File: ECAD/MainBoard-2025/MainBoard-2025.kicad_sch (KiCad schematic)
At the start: 61 parts, among them J1 XT60, J11 Conn_01x04, J12 Conn_01x04, J15 Conn_01x02, J16 XT30, J18 Conn_01x02, J2 Conn_01x04, J20 BAU, J21 BAU, J22 Conn_01x04, J23 Conn_01x02, J26 BAU, J28 Conn_01x02, J3 Conn_01x04, J4 Conn_01x02, J7 XT30, J8 Conn_01x02, J9 Conn_01x02, K2 FINDER-36.11, U2 R-78B3.3-2.0, U3 R-78B12-2.0, U4 R-78B5.0-2.0, U5 Teensy4.1

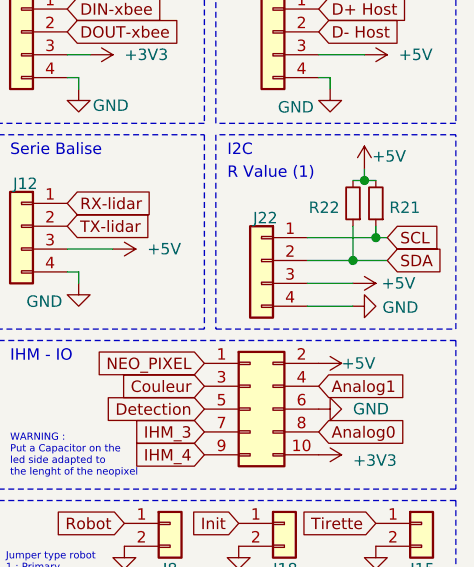
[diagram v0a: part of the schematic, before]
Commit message: new board cut edge and new robot frames
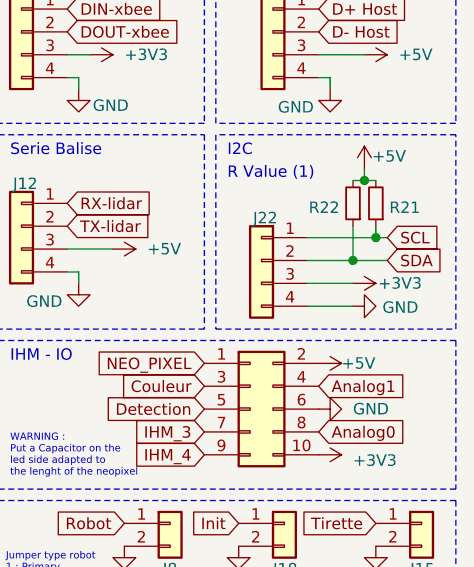
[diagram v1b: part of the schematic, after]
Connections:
- net +3V3: now also J22.3 (Pin_3)
- net +5V: no longer J22.3 (Pin_3)
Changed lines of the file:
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@@
 	)
 	(symbol
+		(lib_id "power:+3V3")
+		(at 271.78 82.55 270)
+		(unit 1)
+		(exclude_from_sim no)
+		(in_bom yes)
+		(on_board yes)
+		(dnp no)
+		(property "Reference" "#PWR044"
+			(at 267.97 82.55 0)
+			(effects
+				(font
+					(size 1.27 1.27)
+				)
+				(hide yes)
+			)
+		)
+		(property "Value" "+3V3"
+			(at 274.574 82.55 90)
+			(effects
+				(font
+					(size 1.27 1.27)
+				)
+				(justify left)
+			)
+		)
+		(property "Footprint" ""
+			(at 271.78 82.55 0)
+			(effects
+				(font
+					(size 1.27 1.27)
+				)
+				(hide yes)
+			)
+		)
+		(property "Datasheet" ""
+			(at 271.78 82.55 0)
+			(effects
+				(font
+					(size 1.27 1.27)
+				)
+				(hide yes)
+			)
+		)
+		(property "Description" ""
+			(at 271.78 82.55 0)
+			(effects
+				(font
+					(size 1.27 1.27)
+				)
+				(hide yes)
+			)
+		)
+		(pin "1"
+		)
+		(instances
+			(project "MainBoard-2025"
+				(path "/b1b0855c-c4b6-47dd-8ac8-2346963564b3"
+					(reference "#PWR044")
+					(unit 1)
+				)
+			)
+		)
+	)
+	(symbol
 		(lib_id "power:+5V")
 		(at 256.54 20.32 270)
@@
 					(unit 1)
 				)
-			)
-		)
-	)
-	(symbol
-		(lib_id "power:+5V")
-		(at 271.78 82.55 270)
-		(unit 1)
-		(exclude_from_sim no)
-		(in_bom yes)
-		(on_board yes)
-		(dnp no)
-		(property "Reference" "#PWR0139"
-			(at 267.97 82.55 0)
-			(effects
-				(font
-					(size 1.27 1.27)
-				)
-				(hide yes)
-			)
-		)
-		(property "Value" "+5V"
-			(at 274.955 82.5429 90)
-			(effects
-				(font
-					(size 1.27 1.27)
-				)
-				(justify left)
-			)
-		)
-		(property "Footprint" ""
-			(at 271.78 82.55 0)
-			(effects
-				(font
-					(size 1.27 1.27)
-				)
-				(hide yes)
-			)
-		)
-		(property "Datasheet" ""
-			(at 271.78 82.55 0)
-			(effects
-				(font
-					(size 1.27 1.27)
-				)
-				(hide yes)
-			)
-		)
-		(property "Description" ""
-			(at 271.78 82.55 0)
-			(effects
-				(font
-					(size 1.27 1.27)
-				)
-				(hide yes)
-			)
-		)
-		(pin "1"
-		)
-		(instances
-			(project "MainBoard-2025"
-				(path "/b1b0855c-c4b6-47dd-8ac8-2346963564b3"
-					(reference "#PWR0139")
-					(unit 1)
-				)

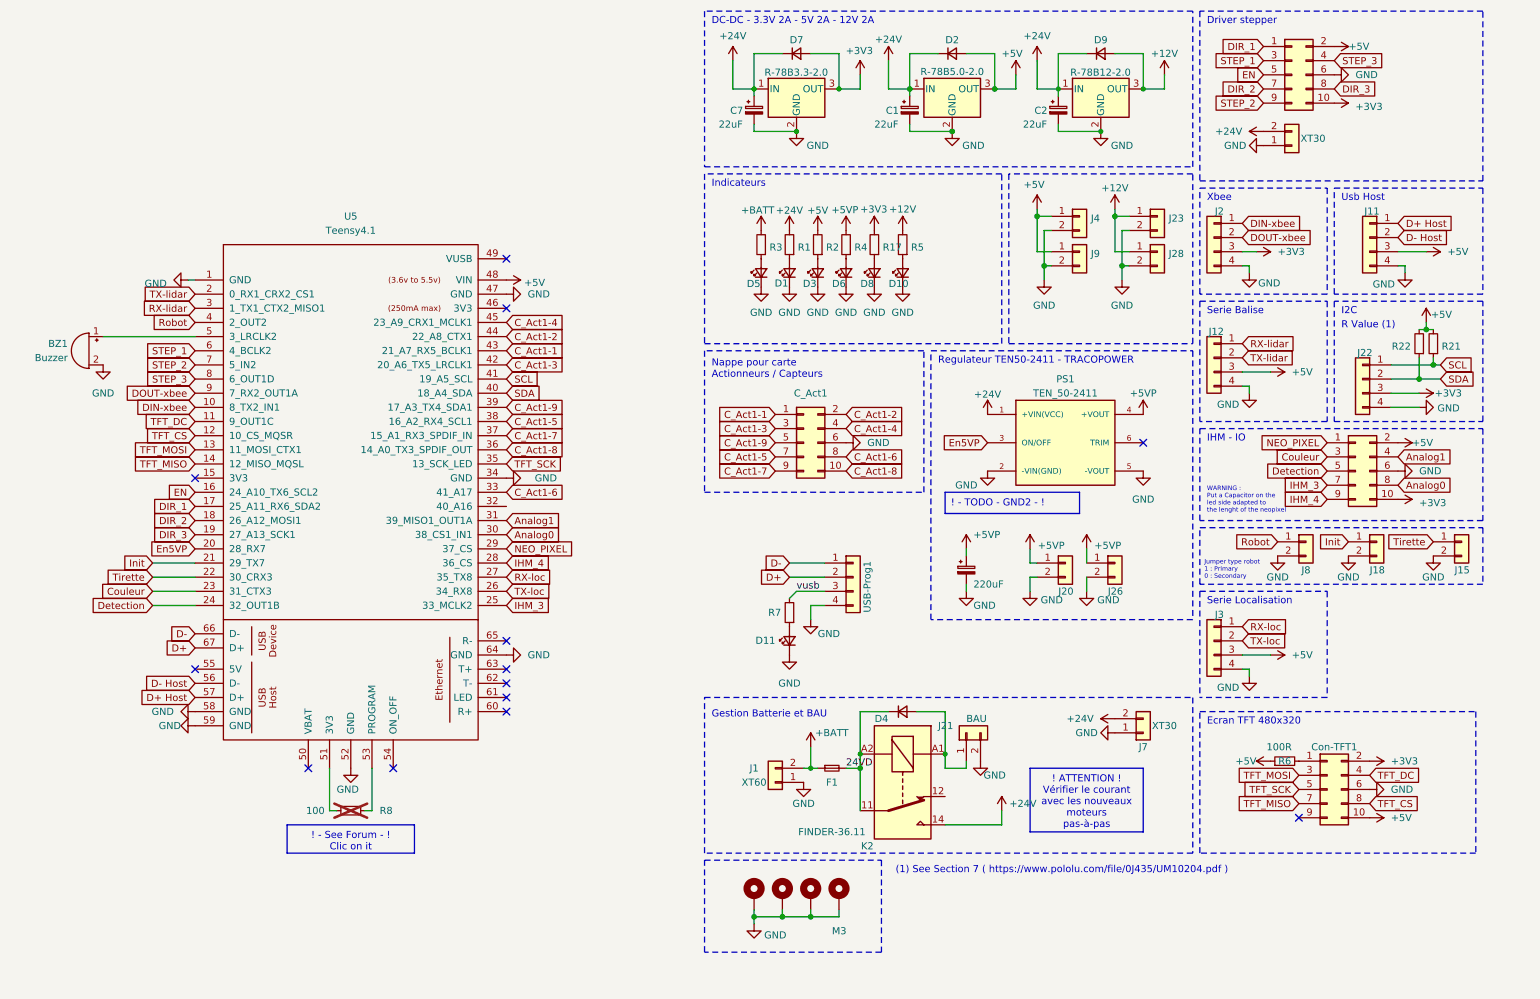
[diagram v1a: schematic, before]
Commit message: Change board size - Move uC - Add connector for Otos sensor
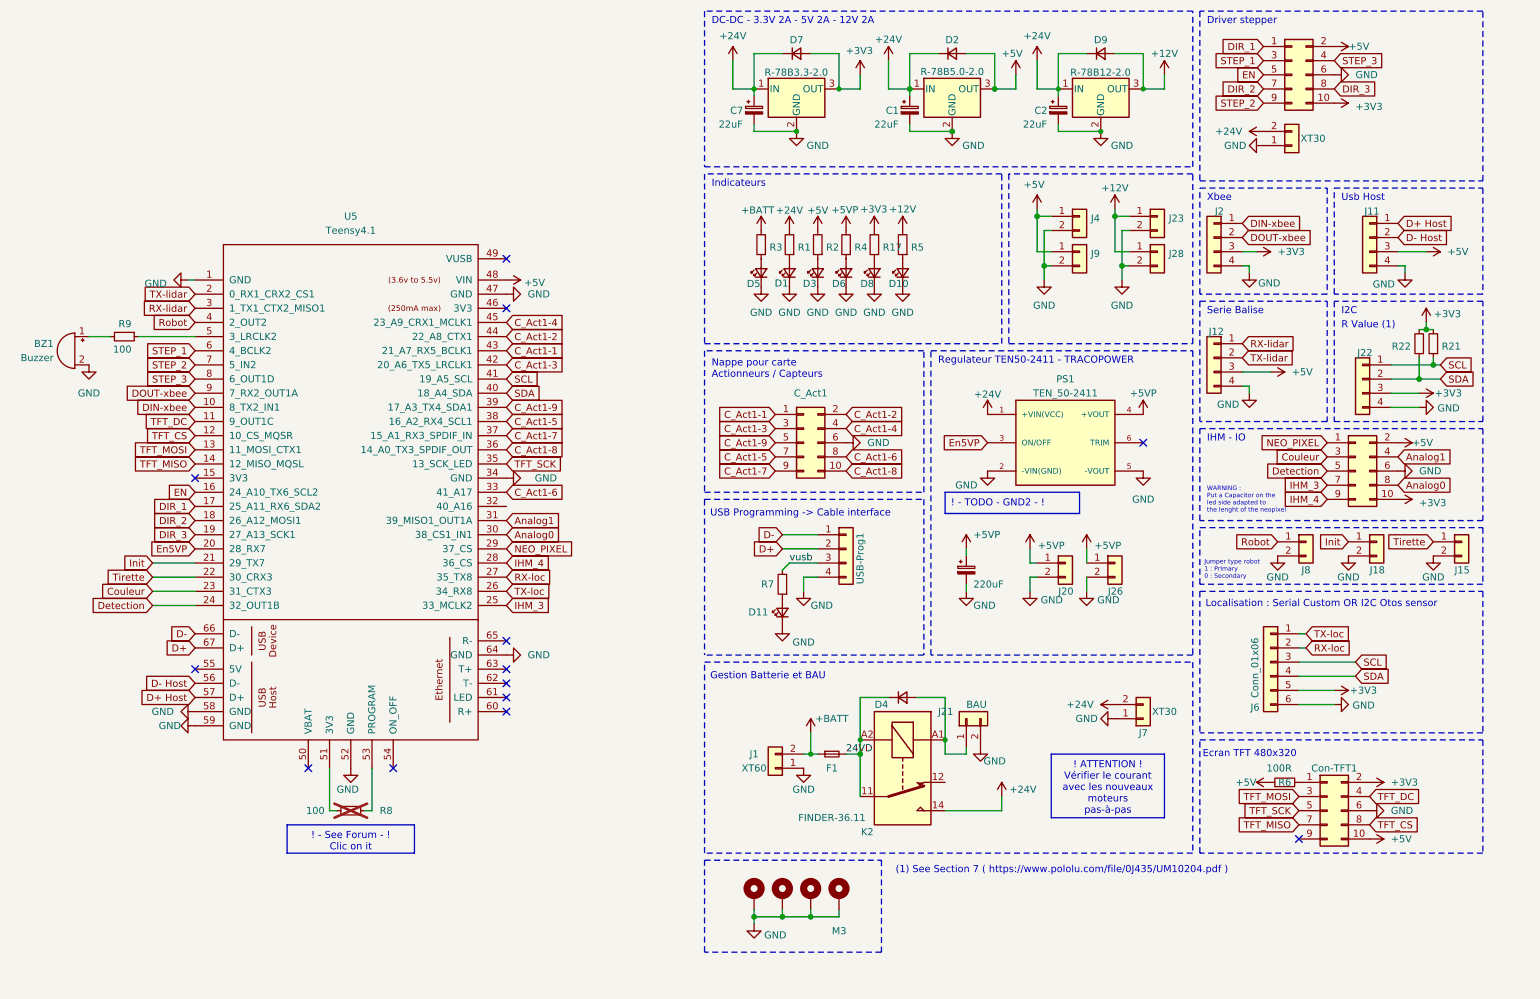
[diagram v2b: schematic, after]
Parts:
- removed J3: Conn_01x04, Connector_Molex:Molex_KK-254_AE-6410-04A_1x04_P2.54mm_Vertical, symbol Connector_Generic:Conn_01x04
- added J6: Conn_01x06, Connector_Molex:Molex_KK-254_AE-6410-06A_1x06_P2.54mm_Vertical, symbol Connector_Generic:Conn_01x06
- added R9: 100, Resistor_SMD:R_1206_3216Metric_Pad1.30x1.75mm_HandSolder, symbol Device:R_Small
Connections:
- net +3V3: now also R21.2, R22.2, J6.5 (Pin_5)
- net +5V: no longer R21.2, R22.2
- net GND: now also J6.6 (Pin_6)
- net RX-loc: now also J6.2 (Pin_2)
- net SCL: now also J6.3 (Pin_3)
- net SDA: now also J6.4 (Pin_4)
- net TX-loc: now also J6.1 (Pin_1)
- net at U5.5 (3_LRCLK2): now also R9.1; no longer BZ1.1 (+)
- new net: BZ1.1 (+), R9.2
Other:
- note added: "Localisation : Serial Custom OR I2C Otos sensor"
- note added: "USB Programming -> Cable interface"
- note removed: "Serie Localisation"
- moved on the sheet: BZ1, Con-TFT1, D11, D4, F1, J1, J21, J7, K2, R6, R7, USB-Prog1

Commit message: Power all the components
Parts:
- removed J11: Conn_01x04, Connector_Molex:Molex_KK-254_AE-6410-04A_1x04_P2.54mm_Vertical, symbol Connector_Generic:Conn_01x04
- added C3: 100uF, Capacitor_SMD:CP_Elec_5x5.4, symbol Device:CP_Small
- added JP1, JP2: SolderJumper_2_Open, Jumper:SolderJumper-2_P1.3mm_Open_RoundedPad1.0x1.5mm, symbol Jumper:SolderJumper_2_Open
- BZ1: footprint (none) -> Buzzer_Beeper:Buzzer_15x7.5RM7.6
- R9: value 100 -> 330
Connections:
- net Buzzer: now reaches R9.1, U5.5 (3_LRCLK2)
- net Buzzer: now also JP1.2 (B)
- net at BZ1.1 (+): now also C3.2, JP2.1 (A); no longer R9.2
- net D+ Host: no longer names the net of U5.57 (D+)
- net D- Host: no longer names the net of U5.56 (D-)
- new net: C3.1, JP1.1 (A), JP2.2 (B), R9.2
- no-connect marks 13 -> 15
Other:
- note removed: "Usb Host"

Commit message: Routing ok - Just before Silkscreen
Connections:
- net DIR_1: now also U5.6 (4_BCLK2); no longer U5.17 (25_A11_RX6_SDA2)
- net DIR_2: now also U5.17 (25_A11_RX6_SDA2); no longer U5.18 (26_A12_MOSI1)
- net DIR_3: now also U5.18 (26_A12_MOSI1); no longer U5.19 (27_A13_SCK1)
- net STEP_1: now also U5.8 (6_OUT1D); no longer U5.6 (4_BCLK2)
- net STEP_2: now also U5.19 (27_A13_SCK1); no longer U5.7 (5_IN2)
- net STEP_3: now also U5.7 (5_IN2); no longer U5.8 (6_OUT1D)

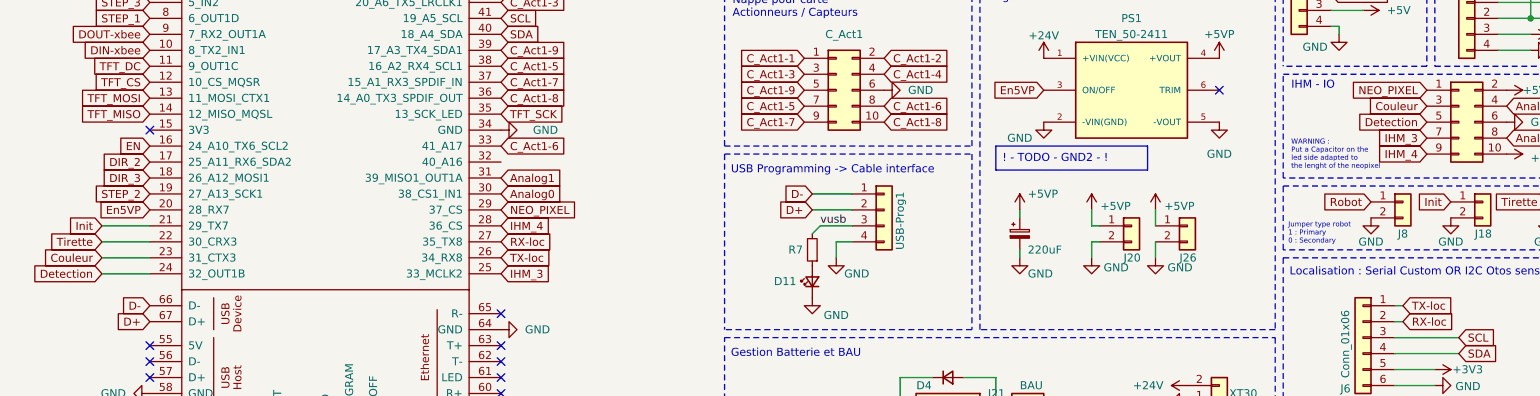
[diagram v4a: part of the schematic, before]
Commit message: WIP - comatibility 3.x 4.x
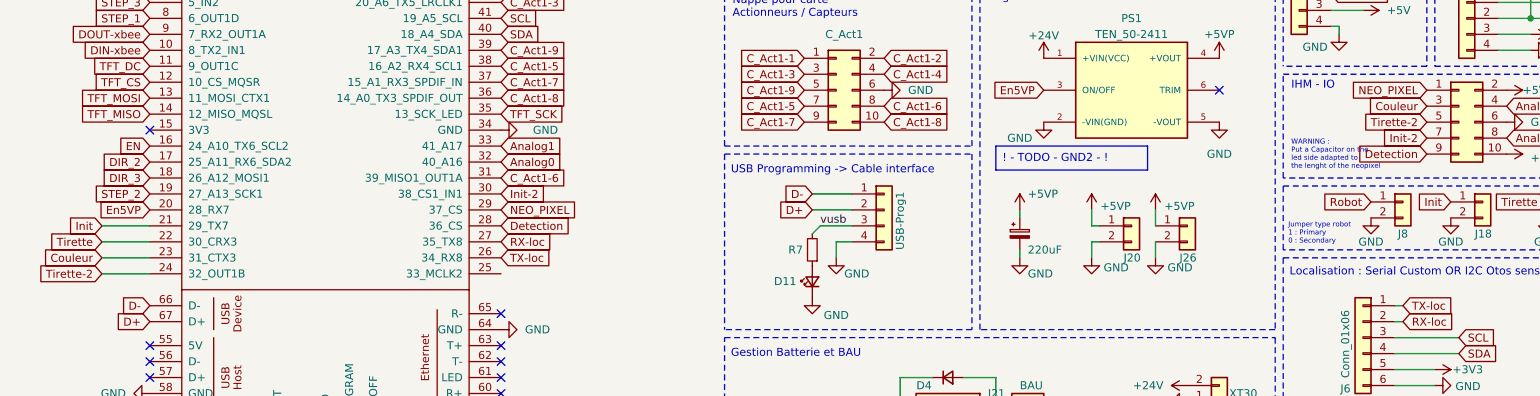
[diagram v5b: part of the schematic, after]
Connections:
- net IHM_4 is gone; now on net Detection: IHM-IO1.9 (Pin_9), U5.28 (36_CS)
- net Analog0: now also U5.32 (40_A16); no longer U5.30 (38_CS1_IN1)
- net Analog1: now also U5.33 (41_A17); no longer U5.31 (39_MISO1_OUT1A)
- net C_Act1-6: now also U5.31 (39_MISO1_OUT1A); no longer U5.33 (41_A17)
- net Detection: no longer IHM-IO1.5 (Pin_5), U5.24 (32_OUT1B)
- net IHM_3: no longer names the net of U5.25 (33_MCLK2)
- net IHM_3: no longer IHM-IO1.7 (Pin_7)
- new net Init-2: IHM-IO1.7 (Pin_7), U5.30 (38_CS1_IN1)
- new net Tirette-2: IHM-IO1.5 (Pin_5), U5.24 (32_OUT1B)

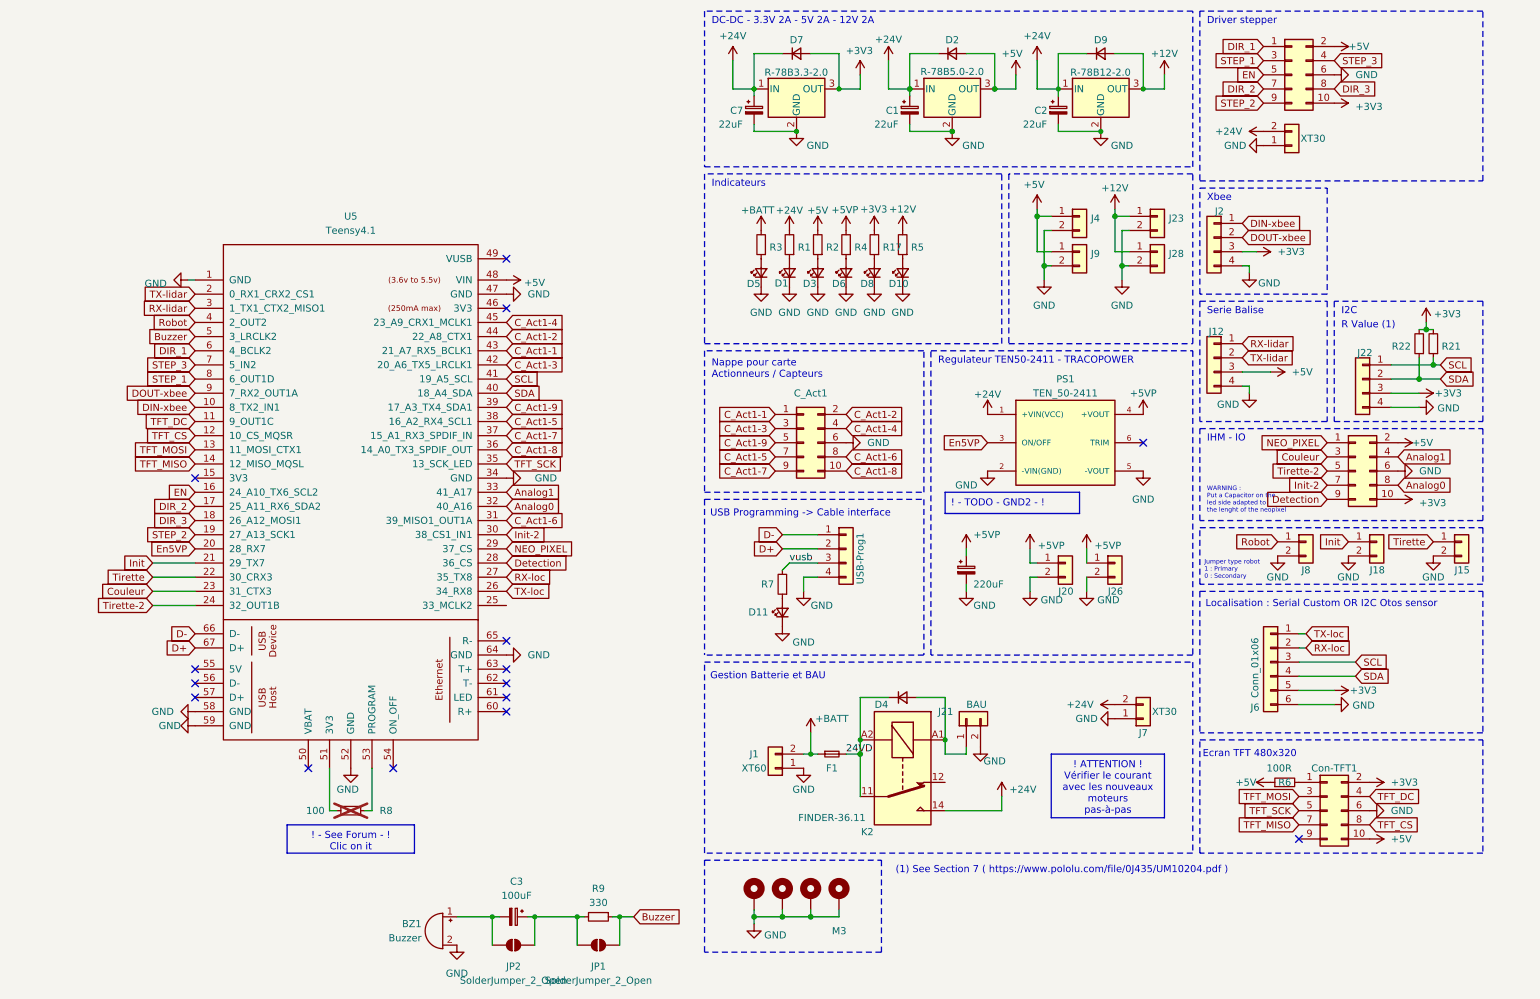
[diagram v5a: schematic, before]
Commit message: Ne Silkscreen - Optimize for 3.5 and 4.1
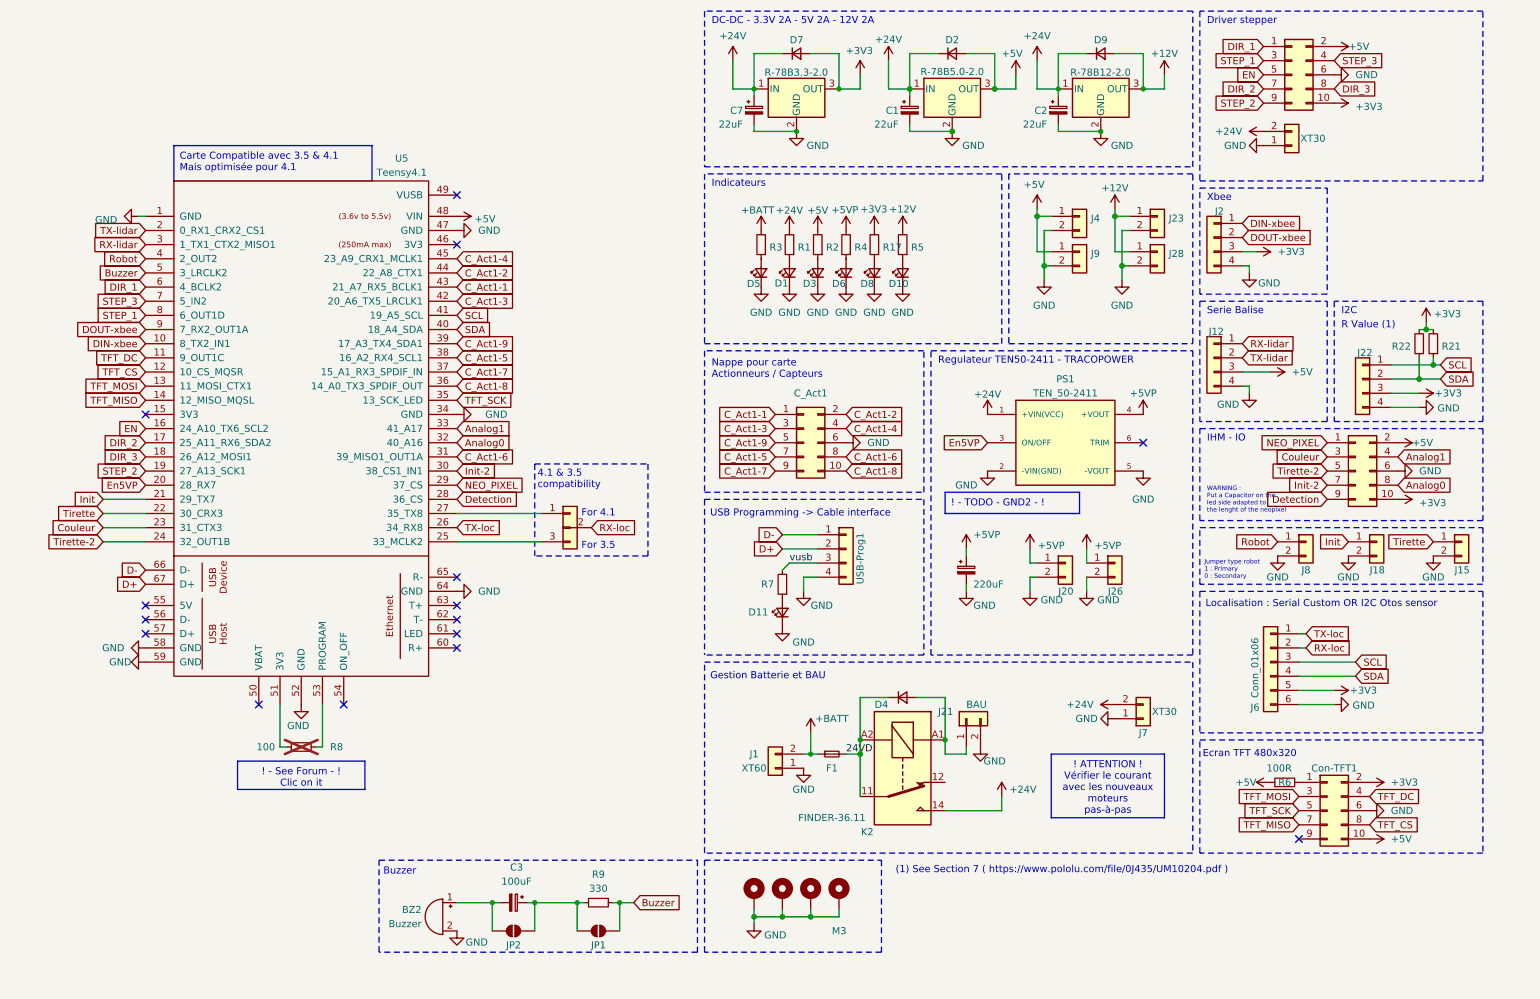
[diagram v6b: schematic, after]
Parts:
- removed BZ1: Buzzer, Buzzer_Beeper:Buzzer_15x7.5RM7.6, symbol Device:Buzzer
- added BZ2: Buzzer, Buzzer_Beeper:Buzzer_12x9.5RM7.6, symbol Device:Buzzer
- added J3: Conn_01x03, Connector_PinHeader_2.54mm:PinHeader_1x03_P2.54mm_Vertical, symbol Connector_Generic:Conn_01x03
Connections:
- net GND: now also BZ2.2 (-)
- net RX-loc: now also J3.2 (Pin_2); no longer U5.27 (35_TX8)
- net at C3.2, JP2.1 (A): now also BZ2.1 (+)
- net at U5.25 (33_MCLK2): now also J3.3 (Pin_3)
- new net: J3.1 (Pin_1), U5.27 (35_TX8)
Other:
- note added: "4.1 & 3.5 compatibility"
- note added: "Buzzer"
- note added: "For 3.5"
- note added: "For 4.1"
- moved on the sheet: C3, JP1, JP2, R8, R9, U5
